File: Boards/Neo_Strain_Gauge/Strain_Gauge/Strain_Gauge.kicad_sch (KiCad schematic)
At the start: 70 parts, among them J1 Screw_Terminal_01x03, J2 Screw_Terminal_01x03, J3 Screw_Terminal_01x03, J4 Screw_Terminal_01x03, J5 Conn_01x02, J6 USB_B_Micro, J7 Conn_02x10_Counter_Clockwise, J8 Conn_02x12_Counter_Clockwise, U1 W25Q128JVS, U2 NCP1117-3.3_SOT223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

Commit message: Swap part for more appropriate to i2c equivalent
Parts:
- U5: Purchase Link https://www.digikey.com/en/products/detail/texas-instruments/TXB0104RGYR/1629103 -> https://www.digikey.com/en/products/detail/texas-instruments/TXS0104ERGYR/1143663
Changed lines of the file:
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@@
       (effects (font (size 1.27 1.27)) hide)
     )
-    (property "Datasheet" "http://www.ti.com/lit/ds/symlink/txb0104.pdf" (id 3) (at 251.714 412.877 0)
+    (property "Datasheet" "https://www.ti.com/lit/ds/symlink/txs0104e.pdf" (id 3) (at 251.714 412.877 0)
       (effects (font (size 1.27 1.27)) hide)
     )
-    (property "Purchase Link" "https://www.digikey.com/en/products/detail/texas-instruments/TXB0104RGYR/1629103" (id 4) (at 248.92 415.29 0)
+    (property "Purchase Link" "https://www.digikey.com/en/products/detail/texas-instruments/TXS0104ERGYR/1143663" (id 4) (at 248.92 415.29 0)
       (effects (font (size 1.27 1.27)) hide)
     )

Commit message: Near finished with BOM selection
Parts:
- C1, C2: Purchase Link (none) -> https://www.digikey.com/en/products/detail/kemet/C0603C270F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
- C10, C8: Purchase Link (none) -> https://www.digikey.com/en/products/detail/taiyo-yuden/EMK1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
- C17: footprint Capacitor_SMD:C_0603_1608Metric -> Capacitor_Tantalum_SMD:CP_EIA-3216-18_Kemet-A; Purchase Link (none) -> https://www.digikey.com/en/products/detail/kyocera-avx/TLJA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
- C18: Purchase Link (none) -> https://www.digikey.com/en/products/detail/tdk-corporation/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
- C19, C24, C27, C28, C29: value 0.1pF -> 100n; footprint Capacitor_SMD:C_0603_1608Metric -> Capacitor_SMD:C_0402_1005Metric; Purchase Link (none) -> https://www.digikey.com/en/products/detail/kyocera-avx/0402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
- C22, C4, C5: Purchase Link (none) -> https://www.digikey.com/en/products/detail/murata-electroni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
- U5: value TXB0104RGY -> TXS0104ERGYR
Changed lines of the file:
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@@
       (effects (font (size 1.27 1.27)) (justify right))
     )
-    (property "Value" "0.1pF" (id 1) (at -218.44 299.7199 0)
+    (property "Value" "100n" (id 1) (at -218.44 299.7199 0)
       (effects (font (size 1.27 1.27)) (justify right))
     )
-    (property "Footprint" "Capacitor_SMD:C_0603_1608Metric" (id 2) (at -224.4852 294.64 0)
+    (property "Footprint" "Capacitor_SMD:C_0402_1005Metric" (id 2) (at -224.4852 294.64 0)
       (effects (font (size 1.27 1.27)) hide)
     )
     (property "Datasheet" "~" (id 3) (at -223.52 298.45 0)
+      (effects (font (size 1.27 1.27)) hide)
+    )
+    (property "Purchase Link" "https://www.digikey.com/en/products/detail/kyocera-avx/04025C104KAT2A/6564238" (id 4) (at -223.52 298.45 0)
       (effects (font (size 1.27 1.27)) hide)
     )
@@
       (effects (font (size 1.27 1.27)) (justify left))
     )
-    (property "Footprint" "Capacitor_SMD:C_0603_1608Metric" (id 2) (at -57.4548 361.95 0)
+    (property "Footprint" "Capacitor_Tantalum_SMD:CP_EIA-3216-18_Kemet-A" (id 2) (at -57.4548 361.95 0)
       (effects (font (size 1.27 1.27)) hide)
     )
     (property "Datasheet" "~" (id 3) (at -58.42 358.14 0)
+      (effects (font (size 1.27 1.27)) hide)
+    )
+    (property "Purchase Link" "https://www.digikey.com/en/products/detail/kyocera-avx/TLJA476M010R0600/3068502" (id 4) (at -58.42 358.14 0)
       (effects (font (size 1.27 1.27)) hide)
     )
@@
     )
     (property "Datasheet" "~" (id 3) (at 229.87 365.76 0)
+      (effects (font (size 1.27 1.27)) hide)
+    )
+    (property "Purchase Link" "https://www.digikey.com/en/products/detail/kemet/C0603C270F3HACAUTO/7956447" (id 4) (at 229.87 365.76 0)
       (effects (font (size 1.27 1.27)) hide)
     )
@@
       (effects (font (size 1.27 1.27)) hide)
     )
+    (property "Purchase Link" "https://www.digikey.com/en/products/detail/taiyo-yuden/EMK105BJ105MVHF/7403763" (id 4) (at 384.81 284.48 0)
+      (effects (font (size 1.27 1.27)) hide)
+    )
     (pin "1")
     (pin "2")
@@
       (effects (font (size 1.27 1.27)) hide)
     )
+    (property "Purchase Link" "https://www.digikey.com/en/products/detail/murata-electronics/GRT188C81A106ME13D/5416705" (id 4) (at 241.3 236.22 0)
+      (effects (font (size 1.27 1.27)) hide)
+    )
     (pin "1")
     (pin "2")
@@
       (effects (font (size 1.27 1.27)) hide)
     )
+    (property "Purchase Link" "https://www.digikey.com/en/products/detail/tdk-corporation/CGA3E3X5R1A225K080AB/3949680" (id 4) (at 74.93 289.56 0)
+      (effects (font (size 1.27 1.27)) hide)
+    )
     (pin "1")
     (pin "2")
@@
       (effects (font (size 1.27 1.27)) (justify right))
     )
-    (property "Value" "0.1pF" (id 1) (at -219.71 267.9699 0)
+    (property "Value" "100n" (id 1) (at -219.71 267.9699 0)
       (effects (font (size 1.27 1.27)) (justify right))
     )
-    (property "Footprint" "Capacitor_SMD:C_0603_1608Metric" (id 2) (at -225.7552 262.89 0)
+    (property "Footprint" "Capacitor_SMD:C_0402_1005Metric" (id 2) (at -225.7552 262.89 0)
       (effects (font (size 1.27 1.27)) hide)
     )
     (property "Datasheet" "~" (id 3) (at -224.79 266.7 0)
+      (effects (font (size 1.27 1.27)) hide)
+    )
+    (property "Purchase Link" "https://www.digikey.com/en/products/detail/kyocera-avx/04025C104KAT2A/6564238" (id 4) (at -224.79 266.7 0)
       (effects (font (size 1.27 1.27)) hide)
     )
@@
       (effects (font (size 1.27 1.27)) (justify left))
     )
-    (property "Value" "TXB0104RGY" (id 1) (at 260.35 398.78 0)
+    (property "Value" "TXS0104ERGYR" (id 1) (at 260.35 398.78 0)
       (effects (font (size 1.27 1.27)) (justify left))
     )
@@
       (effects (font (size 1.27 1.27)) hide)
     )
+    (property "Purchase Link" "https://www.digikey.com/en/products/detail/murata-electronics/GRT188C81A106ME13D/5416705" (id 4) (at 287.02 267.97 0)
+      (effects (font (size 1.27 1.27)) hide)
+    )
     (pin "1")
     (pin "2")
@@
       (effects (font (size 1.27 1.27)) (justify left))
     )
-    (property "Value" "0.1pF" (id 1) (at 105.41 276.8599 0)
-      (effects (font (size 1.27 1.27)) (justify left))
-    )
-    (property "Footprint" "Capacitor_SMD:C_0603_1608Metric" (id 2) (at 102.5652 279.4 0)
+    (property "Value" "100n" (id 1) (at 105.41 276.8599 0)
+      (effects (font (size 1.27 1.27)) (justify left))
+    )
+    (property "Footprint" "Capacitor_SMD:C_0402_1005Metric" (id 2) (at 102.5652 279.4 0)
       (effects (font (size 1.27 1.27)) hide)
     )
     (property "Datasheet" "~" (id 3) (at 101.6 275.59 0)
+      (effects (font (size 1.27 1.27)) hide)
+    )
+    (property "Purchase Link" "https://www.digikey.com/en/products/detail/kyocera-avx/04025C104KAT2A/6564238" (id 4) (at 101.6 275.59 0)
       (effects (font (size 1.27 1.27)) hide)
     )
@@
       (effects (font (size 1.27 1.27)) hide)
     )
+    (property "Purchase Link" "https://www.digikey.com/en/products/detail/kemet/C0603C270F3HACAUTO/7956447" (id 4) (at 229.87 375.92 0)
+      (effects (font (size 1.27 1.27)) hide)
+    )
     (pin "1")
     (pin "2")
@@
       (effects (font (size 1.27 1.27)) hide)
     )
+    (property "Purchase Link" "https://www.digikey.com/en/products/detail/murata-electronics/GRT188C81A106ME13D/5416705" (id 4) (at 251.46 267.97 0)
+      (effects (font (size 1.27 1.27)) hide)
+    )
     (pin "1")
     (pin "2")
@@
     )
     (property "Datasheet" "~" (id 3) (at 330.2 284.48 0)
+      (effects (font (size 1.27 1.27)) hide)
+    )
+    (property "Purchase Link" "https://www.digikey.com/en/products/detail/taiyo-yuden/EMK105BJ105MVHF/7403763" (id 4) (at 330.2 284.48 0)
       (effects (font (size 1.27 1.27)) hide)
     )
@@
       (effects (font (size 1.27 1.27)) (justify right))
     )
-    (property "Value" "0.1pF" (id 1) (at -217.17 370.8399 0)
+    (property "Value" "100n" (id 1) (at -217.17 370.8399 0)
       (effects (font (size 1.27 1.27)) (justify right))
     )
-    (property "Footprint" "Capacitor_SMD:C_0603_1608Metric" (id 2) (at -223.2152 365.76 0)
+    (property "Footprint" "Capacitor_SMD:C_0402_1005Metric" (id 2) (at -223.2152 365.76 0)
       (effects (font (size 1.27 1.27)) hide)
     )
     (property "Datasheet" "~" (id 3) (at -222.25 369.57 0)
+      (effects (font (size 1.27 1.27)) hide)
+    )
+    (property "Purchase Link" "https://www.digikey.com/en/products/detail/kyocera-avx/04025C104KAT2A/6564238" (id 4) (at -222.25 369.57 0)
       (effects (font (size 1.27 1.27)) hide)
     )
@@
       (effects (font (size 1.27 1.27)) (justify right))
     )
-    (property "Value" "0.1pF" (id 1) (at -219.71 335.2799 0)
+    (property "Value" "100n" (id 1) (at -219.71 335.2799 0)
       (effects (font (size 1.27 1.27)) (justify right))
     )
-    (property "Footprint" "Capacitor_SMD:C_0603_1608Metric" (id 2) (at -225.7552 330.2 0)
+    (property "Footprint" "Capacitor_SMD:C_0402_1005Metric" (id 2) (at -225.7552 330.2 0)
       (effects (font (size 1.27 1.27)) hide)
     )
     (property "Datasheet" "~" (id 3) (at -224.79 334.01 0)
+      (effects (font (size 1.27 1.27)) hide)
+    )
+    (property "Purchase Link" "https://www.digikey.com/en/products/detail/kyocera-avx/04025C104KAT2A/6564238" (id 4) (at -224.79 334.01 0)
       (effects (font (size 1.27 1.27)) hide)
     )
@@
     )
     (path "/53341c2b-7d35-467b-b284-185f9ff75f04"
-      (reference "C17") (unit 1) (value "47uF") (footprint "Capacitor_SMD:C_0603_1608Metric")
+      (reference "C17") (unit 1) (value "47uF") (footprint "Capacitor_Tantalum_SMD:CP_EIA-3216-18_Kemet-A")
     )
     (path "/6e18a5b5-6aa5-4791-b0f2-266d784f02f3"
@@
     )
     (path "/a43dc457-f432-443b-9720-94e50b003bee"
-      (reference "C19") (unit 1) (value "0.1pF") (footprint "Capacitor_SMD:C_0603_1608Metric")
+      (reference "C19") (unit 1) (value "100n") (footprint "Capacitor_SMD:C_0402_1005Metric")
     )
     (path "/9cd81dbb-c6dd-4a0c-8510-f8196ca48954"
@@
     )
     (path "/747527fd-7ecf-4728-86f2-2a6062d2def3"
-      (reference "C24") (unit 1) (value "0.1pF") (footprint "Capacitor_SMD:C_0603_1608Metric")
+      (reference "C24") (unit 1) (value "100n") (footprint "Capacitor_SMD:C_0402_1005Metric")
     )
     (path "/dd4ae43c-3ba5-4e39-97ec-37b148192059"
-      (reference "C27") (unit 1) (value "0.1pF") (footprint "Capacitor_SMD:C_0603_1608Metric")
+      (reference "C27") (unit 1) (value "100n") (footprint "Capacitor_SMD:C_0402_1005Metric")
     )
     (path "/342d7914-0b52-4b39-89c0-a664d9b0cceb"
-      (reference "C28") (unit 1) (value "0.1pF") (footprint "Capacitor_SMD:C_0603_1608Metric")
+      (reference "C28") (unit 1) (value "100n") (footprint "Capacitor_SMD:C_0402_1005Metric")
     )
     (path "/d63cdad1-d71a-4e01-9d36-7670901bb266"
-      (reference "C29") (unit 1) (value "0.1pF") (footprint "Capacitor_SMD:C_0603_1608Metric")
+      (reference "C29") (unit 1) (value "100n") (footprint "Capacitor_SMD:C_0402_1005Metric")
     )
     (path "/8131d918-2cde-4f72-88a5-8debebd6aa39"
@@
     )
     (path "/7fb1036e-ad1b-43e8-8de1-603e55ce9732"
-      (reference "U5") (unit 1) (value "TXB0104RGY") (footprint "Package_DFN_QFN:Texas_S-PVQFN-N14")
+      (reference "U5") (unit 1) (value "TXS0104ERGYR") (footprint "Package_DFN_QFN:Texas_S-PVQFN-N14")
     )
     (path "/351c1d0f-6b95-44d8-a946-3dfc3db07878"

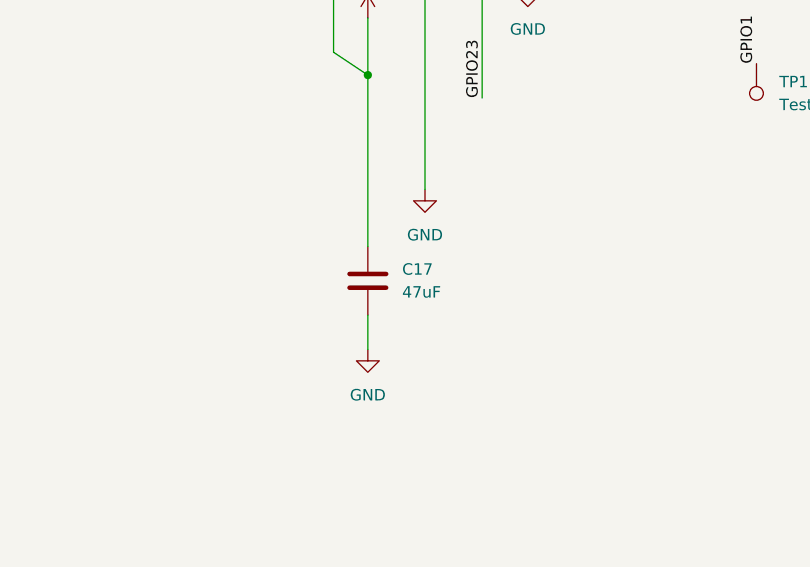
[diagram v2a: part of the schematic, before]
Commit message: Finish basic BOM and update desc. in pcb
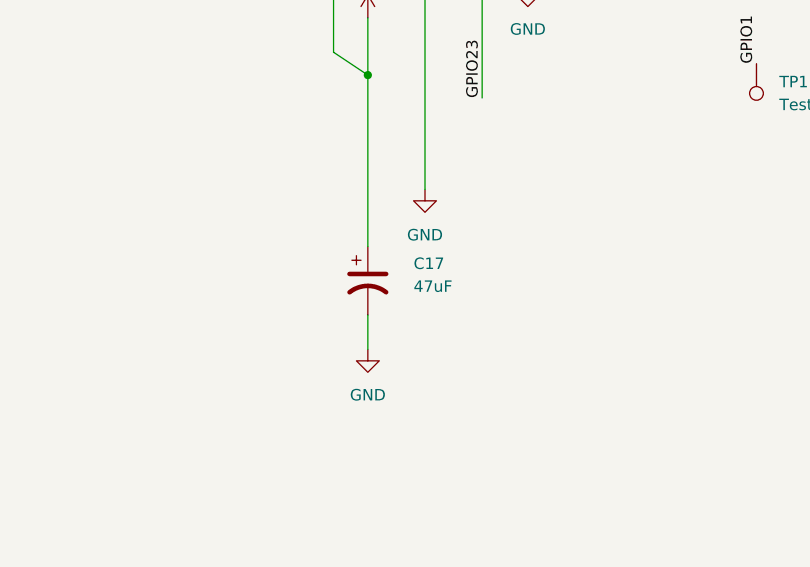
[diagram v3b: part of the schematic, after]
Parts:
- removed C17: 47uF, Capacitor_Tantalum_SMD:CP_EIA-3216-18_Kemet-A, symbol Device:C
- added C17: 47uF, Capacitor_Tantalum_SMD:CP_EIA-3216-18_Kemet-A, symbol Device:C_Polarized_US
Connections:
- net +5V: now also C17.1
- net GND: now also C17.2
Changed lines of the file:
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@@
-    (pin "2")
-  )
-  (symbol (lib_id "Device:C") (at -58.42 358.14 0) (unit 1)
-    (in_bom yes) (on_board yes)
-    (property "Reference" "C17" (id 0) (at -54.61 356.87 0)
-      (effects (font (size 1.27 1.27)) (justify left))
-    )
-    (property "Value" "47uF" (id 1) (at -54.61 359.41 0)
-      (effects (font (size 1.27 1.27)) (justify left))
-    )
-    (property "Footprint" "Capacitor_Tantalum_SMD:CP_EIA-3216-18_Kemet-A" (id 2) (at -57.4548 361.95 0)
-      (effects (font (size 1.27 1.27)) hide)
-    )
-    (property "Datasheet" "~" (id 3) (at -58.42 358.14 0)
-      (effects (font (size 1.27 1.27)) hide)
-    )
-    (property "Purchase Link" "https://www.digikey.com/en/products/detail/kyocera-avx/TLJA476M010R0600/3068502" (id 4) (at -58.42 358.14 0)
-      (effects (font (size 1.27 1.27)) hide)
-    )
-    (pin "1")
     (pin "2")
   )
@@
     (pin "1")
   )
+  (symbol (lib_id "Device:C_Polarized_US") (at -58.42 358.14 0) (unit 1)
+    (in_bom yes) (on_board yes) (fields_autoplaced)
+    (property "Reference" "C17" (id 0) (at -53.34 356.2349 0)
+      (effects (font (size 1.27 1.27)) (justify left))
+    )
+    (property "Value" "47uF" (id 1) (at -53.34 358.7749 0)
+      (effects (font (size 1.27 1.27)) (justify left))
+    )
+    (property "Footprint" "Capacitor_Tantalum_SMD:CP_EIA-3216-18_Kemet-A" (id 2) (at -58.42 358.14 0)
+      (effects (font (size 1.27 1.27)) hide)
+    )
+    (property "Datasheet" "~" (id 3) (at -58.42 358.14 0)
+      (effects (font (size 1.27 1.27)) hide)
+    )
+    (property "Purchase Link" "https://www.digikey.com/en/products/detail/kyocera-avx/TLJA476M010R0600/3068502" (id 4) (at -58.42 358.14 0)
+      (effects (font (size 1.27 1.27)) hide)
+    )
+    (pin "1")
+    (pin "2")
+  )
   (symbol (lib_id "power:GND") (at -231.14 313.69 0) (unit 1)
     (in_bom yes) (on_board yes) (fields_autoplaced)
@@
       (reference "C16") (unit 1) (value "100n") (footprint "Capacitor_SMD:C_0402_1005Metric")
     )
-    (path "/53341c2b-7d35-467b-b284-185f9ff75f04"
+    (path "/d6d1a8be-2fa0-452f-8810-c1b6e248e776"
       (reference "C17") (unit 1) (value "47uF") (footprint "Capacitor_Tantalum_SMD:CP_EIA-3216-18_Kemet-A")
     )
